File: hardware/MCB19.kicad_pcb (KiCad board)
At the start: 2 copper layers, 172.8 x 81.5 mm, 120 parts, among them J401 USART, J402 DISABLE, J601 RJ45, J602 RJ45, J611 +BAT_IN, J612 -BAT_IN, J613 +BAT_OUT, J614 -BAT_OUT, K601 G5LE-1, Q601 IRFP260N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

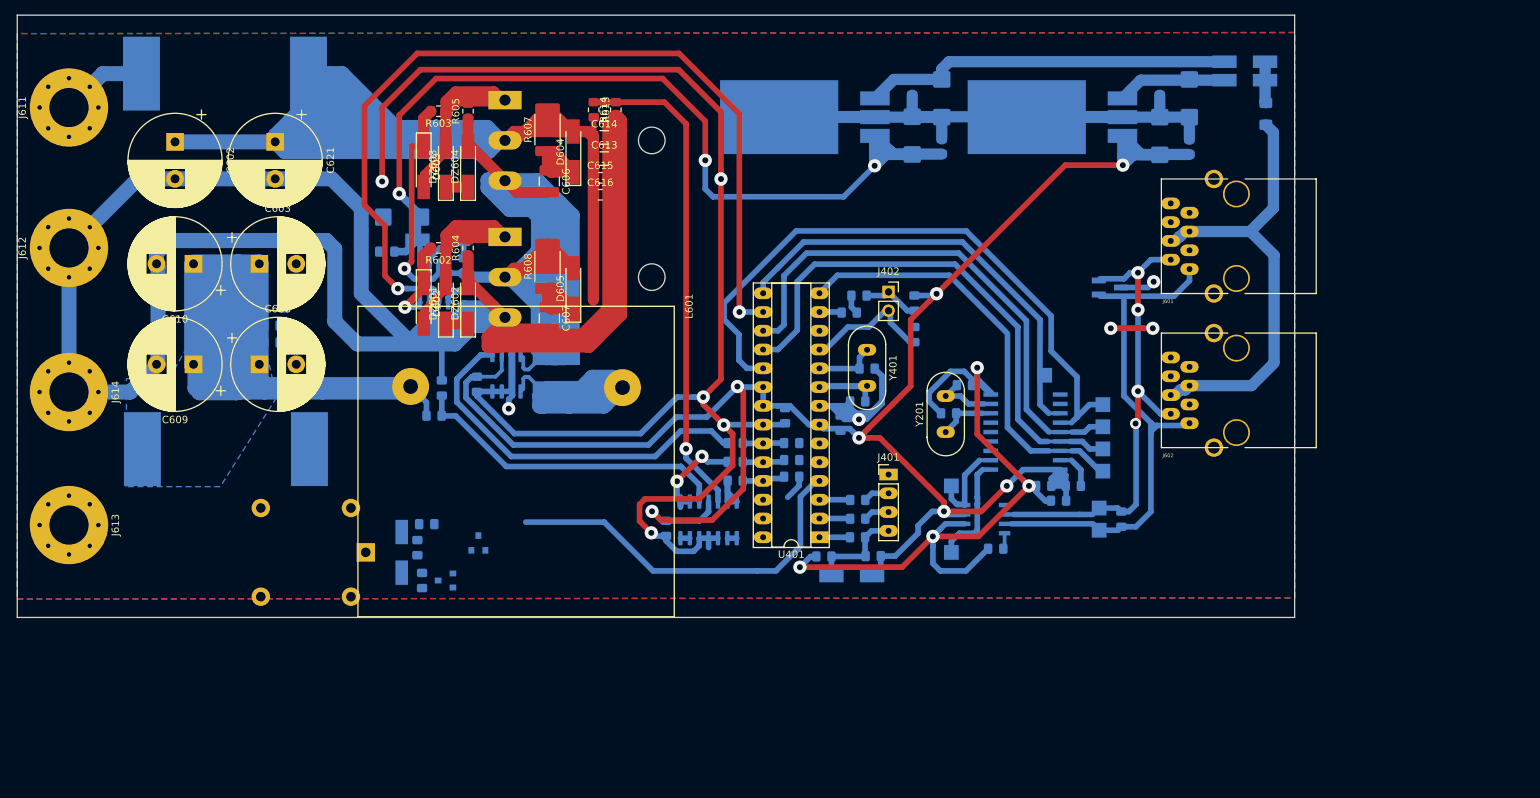
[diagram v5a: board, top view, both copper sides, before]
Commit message: relay finished
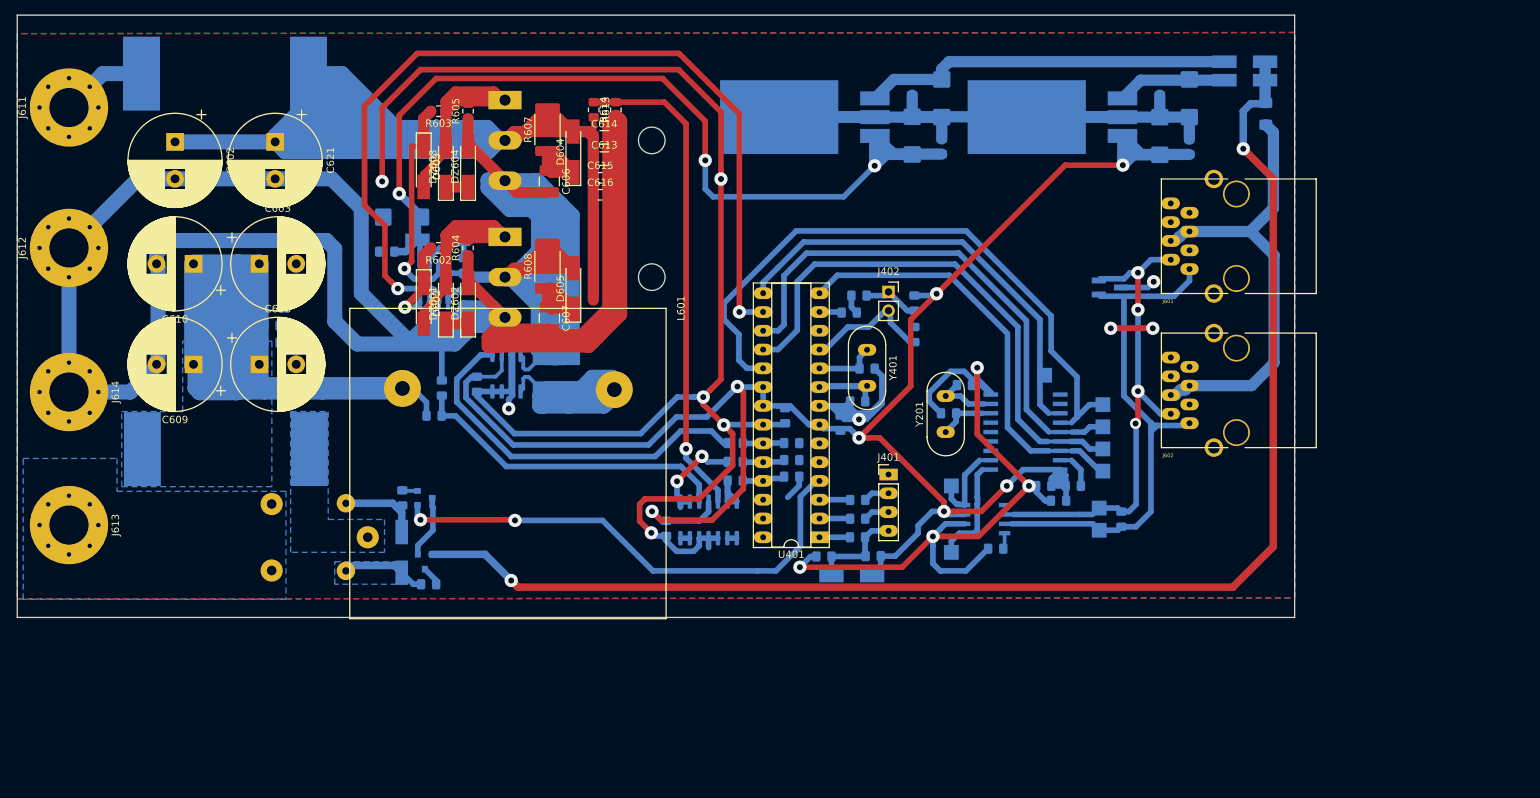
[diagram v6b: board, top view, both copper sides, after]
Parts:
- removed R612: 1k, Resistor_SMD:R_0805_2012Metric_Pad1.15x1.40mm_HandSolder
- K601: footprint Relay_THT:Relay_SPDT_Omron-G5LE-1 -> KicadZeniteSolarLibrary18:Relay_SPDT_SANYOU_SRD_Series_Form_C
- moved Q604 9.46 mm to (105.2, 115.8), turned to 0 degrees
- moved R611 4.85 mm to (102.1, 115.8), turned to 90 degrees
- moved Q603 3.78 mm to (105.2, 124.5), turned to 270 degrees
- moved K601 2.84 mm to (98.4, 120.7), turned to 180 degrees
- moved L601 1.14 mm to (137.8, 90.2)
- moved R1 1.02 mm to (105.7, 127.5), turned to 0 degrees
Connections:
- D301 pad 2: /POWER SUPPLY/+18V_IN -> VCC
- D501 pad 2: /POWER SUPPLY/+18V_IN -> VCC
- F501 pad 1: /POWER SUPPLY/+18V_IN -> VCC
- F501 pad 2: VCC -> /CANBUS CONN/CAN_18V
- J601 pad 4: VCC -> /CANBUS CONN/CAN_18V
- J601 pad 5: VCC -> /CANBUS CONN/CAN_18V
- J602 pad 4: VCC -> /CANBUS CONN/CAN_18V
- J602 pad 5: VCC -> /CANBUS CONN/CAN_18V
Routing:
- net VCC: track 70.6 -> 187.6 mm, vias 0 -> 2
- net /CANBUS CONN/CAN_18V: track 0.00 -> 70.6 mm
- net /MCU/ENABLE: track 51.8 -> 68.3 mm, vias 0 -> 2
- net GND: track 926.0 -> 940.3 mm
- net /driver/relay_coil: track 0.00 -> 11.5 mm
- net Net-(Q603-Pad1): track 0.00 -> 8.52 mm
- net /POWER SUPPLY/+18V_IN: track 5.60 -> 0.00 mm
- net Net-(Q603-Pad3): track 0.00 -> 2.68 mm
- net Net-(Q604-Pad2): track 0.00 -> 2.08 mm
- added copper zone on B.Cu, net /driver/relay_coil
- added copper zone on B.Cu, net Net-(F602-Pad1)
- added copper zone on B.Cu, net Net-(J613-Pad1)

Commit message: Some fixes, ready for heat transfering
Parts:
- added C622: 100n, Capacitor_SMD:C_0805_2012Metric_Pad1.15x1.40mm_HandSolder, F.Cu at (129.0, 79.6)
- added C623: 100n, Capacitor_SMD:C_0805_2012Metric_Pad1.15x1.40mm_HandSolder, F.Cu at (129.0, 77.2)
- added C624: 100n, Capacitor_SMD:C_0805_2012Metric_Pad1.15x1.40mm_HandSolder, F.Cu at (129.0, 82.0)
- added C625: 100n, Capacitor_SMD:C_0805_2012Metric_Pad1.15x1.40mm_HandSolder, F.Cu at (129.0, 84.4)
- added C626: 100n, Capacitor_SMD:C_0805_2012Metric_Pad1.15x1.40mm_HandSolder, F.Cu at (129.0, 86.8)
- added C627: 100n, Capacitor_SMD:C_0805_2012Metric_Pad1.15x1.40mm_HandSolder, F.Cu at (129.0, 89.2)
- added C628: 1uF, Capacitor_Tantalum_SMD:CP_EIA-6032-20_AVX-F_Pad2.25x2.35mm_HandSolder, B.Cu at (102.0, 124.2)
- added C629: 100nF, Capacitor_SMD:C_0805_2012Metric_Pad1.15x1.40mm_HandSolder, B.Cu at (99.4, 120.6)
- added D402: LED_RED, LED_SMD:LED_0805_2012Metric_Pad1.15x1.40mm_HandSolder, B.Cu at (163.6, 113.0)
- added D607: LED_RED, LED_SMD:LED_0805_2012Metric_Pad1.15x1.40mm_HandSolder, F.Cu at (141.4, 125.2)
- added D608: LED_RED, LED_SMD:LED_0805_2012Metric_Pad1.15x1.40mm_HandSolder, F.Cu at (65.3, 108.8)
- added R404: 330, Resistor_SMD:R_0805_2012Metric_Pad1.15x1.40mm_HandSolder, B.Cu at (163.6, 110.0)
- added R615: 10R, Resistor_SMD:R_2512_6332Metric, F.Cu at (121.8, 66.0)
- added R616: 330, Resistor_SMD:R_0805_2012Metric_Pad1.15x1.40mm_HandSolder, F.Cu at (143.4, 123.0)
- added R617: 10R, Resistor_SMD:R_2512_6332Metric_Pad1.52x3.35mm_HandSolder, F.Cu at (121.8, 84.5)
- added R618: 330, Resistor_SMD:R_0805_2012Metric_Pad1.15x1.40mm_HandSolder, F.Cu at (68.6, 109.8)
- added TP401: PWM, TestPoint:TestPoint_Pad_2.0x2.0mm, F.Cu at (153.2, 79.0)
- added TP402: ENABLE, TestPoint:TestPoint_Pad_2.0x2.0mm, F.Cu at (147.0, 125.0)
- DZ601, DZ602, DZ603, DZ604: value 15V -> 12V
- K601: moved to F.Cu
- R201: value 120 -> 1k
- R601: value 100k -> 50k
- R602, R603: value 1R -> 4R7
- R607, R608: value 1R -> 10R
- moved D606 22.9 mm to (83.8, 109.4), turned to 270 degrees
- moved R612 16.1 mm to (95.6, 115.0), turned to 270 degrees
- moved F602 14.6 mm to (89.2, 123.8)
- moved K601 12.3 mm to (90.8, 111.0)
- moved Q603 10.9 mm to (98.8, 115.5), turned to 180 degrees
- moved R611 2.53 mm to (103.0, 118.2), turned to 0 degrees
- moved Q604 2.48 mm to (103.0, 114.6), turned to 180 degrees
- moved C609 1.34 mm to (74.5, 96.5)
- moved L601 1.26 mm to (139.0, 89.8)
- moved C608 1.20 mm to (82.8, 96.5)
- moved C617 1.00 mm to (84.5, 88.9)
- moved C618 1.00 mm to (84.5, 86.0)
- moved C619 1.00 mm to (84.5, 93.8)
- moved C620 1.00 mm to (84.5, 91.5)
- moved C610 0.96 mm to (74.5, 83.4)
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- renumbered R1 to R612
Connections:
- F602 pad 2: Net-(C603-Pad1) -> Net-(F602-Pad2)
- J613 pad 1: Net-(J613-Pad1) -> Net-(F602-Pad2)
- K601 pad 1: Net-(F602-Pad1) -> Net-(C603-Pad1)
- K601 pad 3: Net-(J613-Pad1) -> Net-(F602-Pad1)
- U201 pad 5: Net-(U201-Pad5) -> (no net)
- U202 pad 10: Net-(U202-Pad10) -> (no net)
- U202 pad 11: Net-(U202-Pad11) -> (no net)
- U202 pad 3: Net-(U202-Pad3) -> (no net)
- U202 pad 4: Net-(U202-Pad4) -> (no net)
- U202 pad 5: Net-(U202-Pad5) -> (no net)
- U202 pad 6: Net-(U202-Pad6) -> (no net)
- U401 pad 12: Net-(U401-Pad12) -> (no net)
- U401 pad 26: Net-(U401-Pad26) -> (no net)
- U401 pad 27: Net-(U401-Pad27) -> (no net)
- U401 pad 28: Net-(U401-Pad28) -> (no net)
- U401 pad 5: Net-(U401-Pad5) -> (no net)
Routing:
- net +BATT: track 298.2 -> 599.5 mm
- net Net-(F602-Pad1): track 0.00 -> 247.5 mm, vias 0 -> 1
- net Net-(C603-Pad1): track 249.2 -> 390.4 mm
- net GND: track 940.3 -> 856.1 mm, vias 14 -> 19
- net /MCU/ENABLE: track 68.3 -> 82.7 mm, vias 2 -> 1
- net /driver/relay_coil: track 11.5 -> 19.2 mm
- net Net-(Q603-Pad1): track 8.52 -> 2.20 mm
- net /MCU/PWM: track 120.6 -> 125.5 mm
- net VCC: track 187.6 -> 182.8 mm
- net Net-(R404-Pad1): track 0.00 -> 4.67 mm
- net Net-(D402-Pad2): track 0.00 -> 3.85 mm
- net Net-(D608-Pad2): track 0.00 -> 2.40 mm
- net Net-(D607-Pad2): track 0.00 -> 2.21 mm
- net +12V: track 135.7 -> 136.5 mm
- net Net-(Q604-Pad2): track 2.08 -> 2.65 mm
- added copper zone on B.Cu, net Net-(F601-Pad2)
- added copper zone on F.Cu, net Net-(F601-Pad2)
- added copper zone on B.Cu, net Net-(F602-Pad2)
- added copper zone on F.Cu, net Net-(F602-Pad2)
- removed copper zone on B.Cu, net /driver/relay_coil
- removed copper zone on B.Cu, net Net-(C603-Pad1)
- removed copper zone on B.Cu, net Net-(F602-Pad1)
- removed copper zone on B.Cu, net Net-(J613-Pad1)

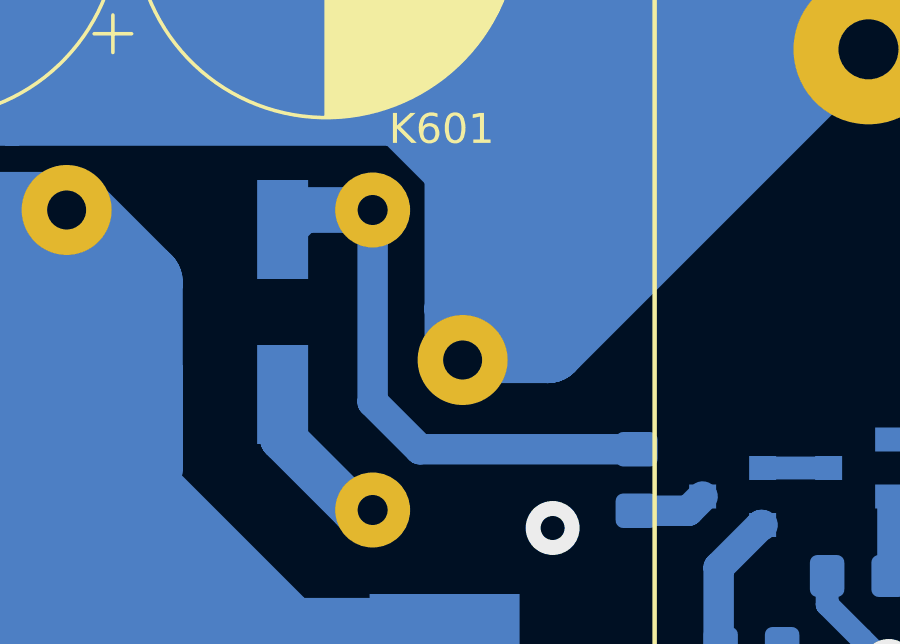
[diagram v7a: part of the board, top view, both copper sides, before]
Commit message: relay pin 1 fixed
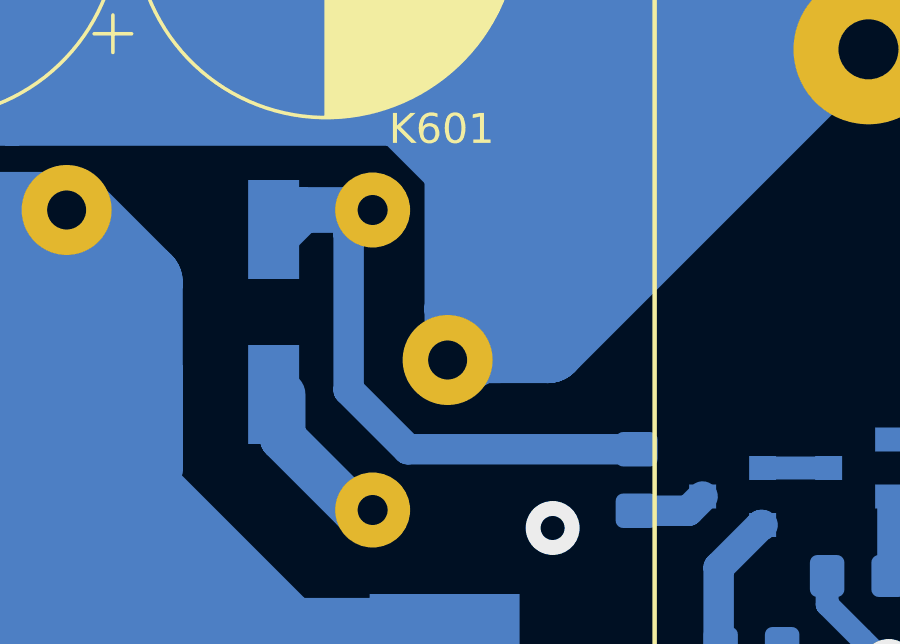
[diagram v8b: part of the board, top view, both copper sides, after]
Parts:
- moved D606 0.30 mm to (83.5, 109.4)
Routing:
- net /driver/relay_coil: track 19.2 -> 20.1 mm
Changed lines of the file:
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@@
     (thickness 1.6)
     (drawings 6)
-    (tracks 1351)
+    (tracks 1352)
     (zones 0)
     (modules 137)
@@
   )
   (setup
-    (last_trace_width 2.54)
+    (last_trace_width 0.508)
     (user_trace_width 0.254)
     (user_trace_width 0.381)
@@
     (diff_pair_gap 0.508)
   )
+  (module KicadZeniteSolarLibrary18:Relay_SPDT_SANYOU_SRD_Series_Form_C (layer F.Cu)
+    (at 90.8 111 180)
+    (descr "relay Sanyou SRD series Form C http://www.sanyourelay.ca/public/products/pdf/SRD.pdf")
+    (tags "relay Sanyu SRD form C")
+    (fp_text reference K601 (at 1.7 7.7 180) (layer F.SilkS)
+      (effects (font (size 1 1) (thickness 0.15)))
+    )
+    (fp_text value G5LE-1 (at 8 -9.6 180) (layer F.Fab)
+      (effects (font (size 1 1) (thickness 0.15)))
+    )
+    (fp_line (start -0.25 6.25) (end 15.45 6.26) (layer F.CrtYd) (width 0.05))
+    (fp_line (start 15.45 6.26) (end 15.45 -6.25) (layer F.CrtYd) (width 0.05))
+    (fp_line (start -0.25 6.25) (end -0.25 -6.25) (layer F.CrtYd) (width 0.05))
+    (fp_line (start 15.45 -6.25) (end -0.25 -6.25) (layer F.CrtYd) (width 0.05))
+    (fp_line (start 0 6) (end 0 -6) (layer F.Fab) (width 0.12))
+    (fp_line (start 15.2 6) (end 0 6) (layer F.Fab) (width 0.12))
+    (fp_line (start 15.2 -6) (end 15.2 6) (layer F.Fab) (width 0.12))
+    (fp_line (start 0 -6) (end 15.2 -6) (layer F.Fab) (width 0.12))
+    (fp_text user 1 (at 0.7 -2.3 180) (layer F.Fab)
+      (effects (font (size 1 1) (thickness 0.15)))
+    )
+    (pad 1 thru_hole circle (at 1.5 0 270) (size 3 3) (drill 1.3) (layers *.Cu *.Mask)
+      (net 26 "Net-(C603-Pad1)"))
+    (pad 5 thru_hole circle (at 4 -5 270) (size 2.5 2.5) (drill 1) (layers *.Cu *.Mask)
+      (net 1 GND))
+    (pad 3 thru_hole circle (at 14.2 5 270) (size 3 3) (drill 1.3) (layers *.Cu *.Mask)
+      (net 62 "Net-(F602-Pad1)"))
+    (pad 2 thru_hole circle (at 4 5 270) (size 2.5 2.5) (drill 1) (layers *.Cu *.Mask)
+      (net 57 /driver/relay_coil))
+    (model ${KISYS3DMOD}/Relay_THT.3dshapes/Relay_SPDT_SANYOU_SRD_Series_Form_C.wrl
+      (at (xyz 0 0 0))
+      (scale (xyz 1 1 1))
+      (rotate (xyz 0 0 0))
+    )
+  )
   (module TestPoint:TestPoint_Pad_2.0x2.0mm (layer F.Cu)
     (at 147 125)
@@
     )
   )
-  (module KicadZeniteSolarLibrary18:Relay_SPDT_SANYOU_SRD_Series_Form_C (layer F.Cu)
-    (at 90.8 111 180)
-    (descr "relay Sanyou SRD series Form C http://www.sanyourelay.ca/public/products/pdf/SRD.pdf")
-    (tags "relay Sanyu SRD form C")
-    (fp_text reference K601 (at 1.7 7.7) (layer F.SilkS)
-      (effects (font (size 1 1) (thickness 0.15)))
-    )
-    (fp_text value G5LE-1 (at 8 -9.6) (layer F.Fab)
-      (effects (font (size 1 1) (thickness 0.15)))
-    )
-    (fp_line (start -0.25 6.25) (end 15.45 6.26) (layer F.CrtYd) (width 0.05))
-    (fp_line (start 15.45 6.26) (end 15.45 -6.25) (layer F.CrtYd) (width 0.05))
-    (fp_line (start -0.25 6.25) (end -0.25 -6.25) (layer F.CrtYd) (width 0.05))
-    (fp_line (start 15.45 -6.25) (end -0.25 -6.25) (layer F.CrtYd) (width 0.05))
-    (fp_line (start 0 6) (end 0 -6) (layer F.Fab) (width 0.12))
-    (fp_line (start 15.2 6) (end 0 6) (layer F.Fab) (width 0.12))
-    (fp_line (start 15.2 -6) (end 15.2 6) (layer F.Fab) (width 0.12))
-    (fp_line (start 0 -6) (end 15.2 -6) (layer F.Fab) (width 0.12))
-    (fp_text user 1 (at 0.7 -2.3) (layer F.Fab)
-      (effects (font (size 1 1) (thickness 0.15)))
-    )
-    (pad 1 thru_hole circle (at 1 0 270) (size 3 3) (drill 1.3) (layers *.Cu *.Mask)
-      (net 26 "Net-(C603-Pad1)"))
-    (pad 5 thru_hole circle (at 4 -5 270) (size 2.5 2.5) (drill 1) (layers *.Cu *.Mask)
-      (net 1 GND))
-    (pad 3 thru_hole circle (at 14.2 5 270) (size 3 3) (drill 1.3) (layers *.Cu *.Mask)
-      (net 62 "Net-(F602-Pad1)"))
-    (pad 2 thru_hole circle (at 4 5 270) (size 2.5 2.5) (drill 1) (layers *.Cu *.Mask)
-      (net 57 /driver/relay_coil))
-    (model ${KISYS3DMOD}/Relay_THT.3dshapes/Relay_SPDT_SANYOU_SRD_Series_Form_C.wrl
-      (at (xyz 0 0 0))
-      (scale (xyz 1 1 1))
-      (rotate (xyz 0 0 0))
-    )
-  )
   (module Resistor_SMD:R_0805_2012Metric_Pad1.15x1.40mm_HandSolder (layer B.Cu)
     (at 102.975 118.2)
@@
   )
   (module Diode_SMD:D_MiniMELF_Handsoldering (layer B.Cu)
-    (at 83.8 109.4 270)
+    (at 83.5 109.4 270)
     (descr "Diode Mini-MELF Handsoldering")
     (tags "Diode Mini-MELF Handsoldering")
@@
   (segment (start 84.45 106) (end 83.8 106.65) (width 1.524) (layer B.Cu) (net 57))
   (segment (start 86.8 106) (end 84.45 106) (width 1.524) (layer B.Cu) (net 57))
-  (segment (start 95.6 113.975) (end 88.375 113.975) (width 1.016) (layer B.Cu) (net 57))
-  (segment (start 86.8 112.4) (end 86.8 106) (width 1.016) (layer B.Cu) (net 57))
-  (segment (start 88.375 113.975) (end 86.8 112.4) (width 1.016) (layer B.Cu) (net 57))
+  (segment (start 86 112) (end 86 106.8) (width 1.016) (layer B.Cu) (net 57))
+  (segment (start 86 106.8) (end 86.8 106) (width 1.016) (layer B.Cu) (net 57))
+  (segment (start 95.6 113.975) (end 87.975 113.975) (width 1.016) (layer B.Cu) (net 57))
+  (segment (start 87.975 113.975) (end 86 112) (width 1.016) (layer B.Cu) (net 57))
   (segment (start 141.01 121.275) (end 139.74 121.275) (width 0.762) (layer B.Cu) (net 58))
   (segment (start 147.36 121.275) (end 146.09 121.275) (width 0.762) (layer B.Cu) (net 59))
